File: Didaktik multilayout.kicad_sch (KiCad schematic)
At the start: 119 parts, among them J1 Conn_01x04_MountingPin, J2 AVR-ISP-6, SW1 SW_Push_45deg, SW10 SW_Push_45deg, SW11 SW_Push_45deg, SW12 SW_Push_45deg, SW13 SW_Push_45deg, SW14 SW_Push_45deg, SW15 SW_Push_45deg, SW16 SW_Push_45deg, SW17 SW_Push_45deg, SW18 SW_Push_45deg, SW19 SW_Push_45deg, SW2 SW_Push_45deg, SW20 SW_Push_45deg, SW21 SW_Push_45deg, SW22 SW_Push_45deg, SW23 SW_Push_45deg, SW24 SW_Push_45deg, SW25 SW_Push_45deg, SW26 SW_Push_45deg, SW27 SW_Push_45deg, SW28 SW_Push_45deg, SW29 SW_Push_45deg, SW3 SW_Push_45deg, SW30 SW_Push_45deg, SW31 SW_Push_45deg, SW31a1 SW_Push_45deg, SW32 SW_Push_45deg, SW32a1 SW_Push_45deg, SW33 SW_Push_45deg, SW33a1 SW_Push_45deg, SW34 SW_Push_45deg, SW34a1 SW_Push_45deg, SW34b1 SW_Push_45deg, SW35 SW_Push_45deg, SW35a1 SW_Push_45deg, SW35b1 SW_Push_45deg, SW35c1 SW_Push_45deg, SW36 SW_Push_45deg, SW36a1 SW_Push_45deg, SW36b1 SW_Push_45deg, SW36c1 SW_Push_45deg, SW37 SW_Push_45deg, SW37a1 SW_Push_45deg, SW37b1 SW_Push_45deg, SW38 SW_Push_45deg, SW38a1 SW_Push_45deg, SW39 SW_Push_45deg, SW39a1 SW_Push_45deg, SW4 SW_Push_45deg, SW40 SW_Push_45deg, SW40a1 SW_Push_45deg, SW5 SW_Push_45deg, SW6 SW_Push_45deg, SW7 SW_Push_45deg, SW8 SW_Push_45deg, SW9 SW_Push_45deg, U1 ATmega32U4-M, Y1 Crystal_GND24_Small

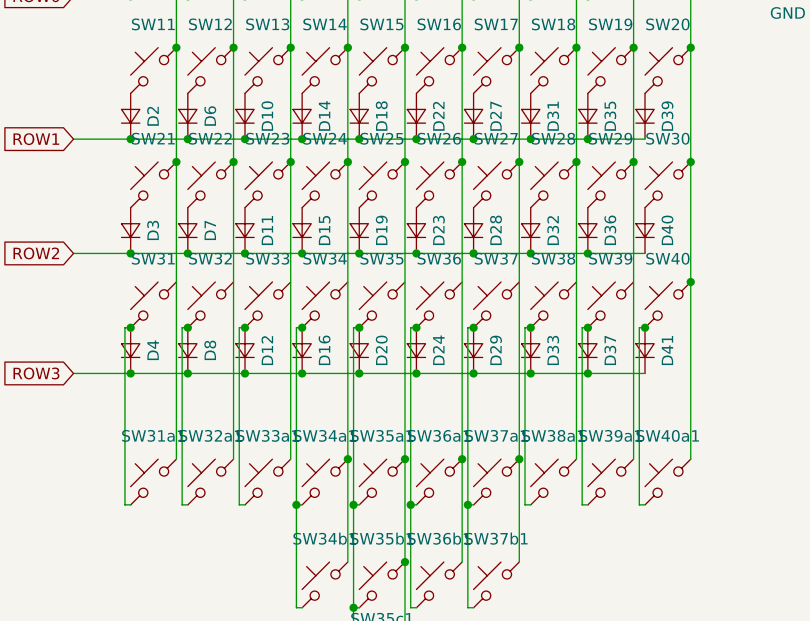
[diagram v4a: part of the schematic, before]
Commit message: routing new simpler matrix on pcb
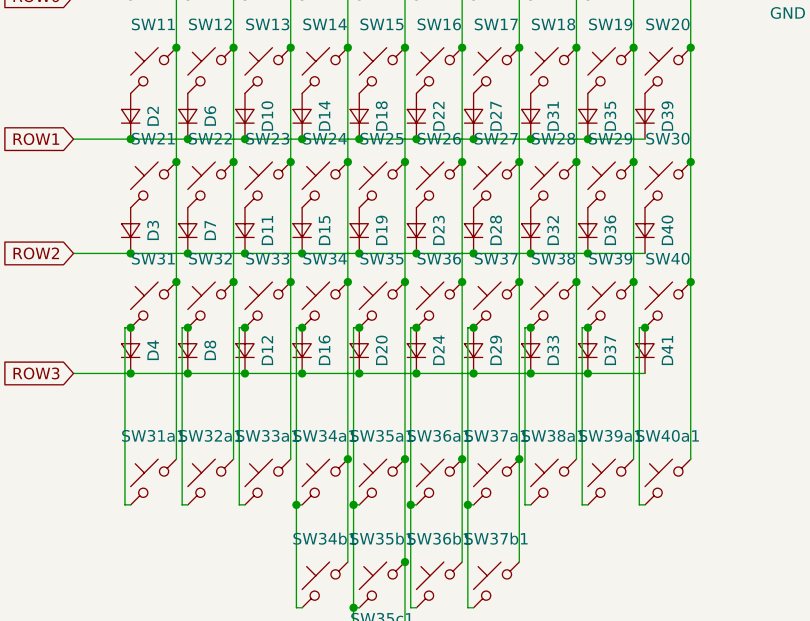
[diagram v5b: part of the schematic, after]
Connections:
- net COL0: now also SW31.1
- net COL1: now also SW32.1
- net COL2: now also SW33.1
- net COL3: now also SW34.1
- net COL4: now also SW35.1
- net COL5: now also SW36.1
- net COL6: now also SW37.1
- net COL7: now also SW38.1
- net COL8: now also SW39.1
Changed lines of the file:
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@@
   (junction (at 116.84 156.21) (diameter 0) (color 0 0 0 0)
   )
+  (junction (at 214.63 83.185) (diameter 0) (color 0 0 0 0)
+  )
   (junction (at 156.21 160.655) (diameter 0) (color 0 0 0 0)
   )
@@
   (junction (at 201.93 41.275) (diameter 0) (color 0 0 0 0)
   )
+  (junction (at 189.23 83.185) (diameter 0) (color 0 0 0 0)
+  )
   (junction (at 116.84 151.13) (diameter 0) (color 0 0 0 0)
   )
@@
   (junction (at 152.4 155.575) (diameter 0) (color 0 0 0 0)
   )
+  (junction (at 176.53 83.185) (diameter 0) (color 0 0 0 0)
+  )
   (junction (at 171.45 80.01) (diameter 0) (color 0 0 0 0)
   )
@@
   (junction (at 177.8 93.345) (diameter 0) (color 0 0 0 0)
   )
+  (junction (at 201.93 83.185) (diameter 0) (color 0 0 0 0)
+  )
   (junction (at 209.55 51.435) (diameter 0) (color 0 0 0 0)
   )
@@
   (junction (at 171.45 67.31) (diameter 0) (color 0 0 0 0)
   )
+  (junction (at 170.18 83.185) (diameter 0) (color 0 0 0 0)
+  )
   (junction (at 196.85 88.265) (diameter 0) (color 0 0 0 0)
   )
@@
   (junction (at 160.02 160.655) (diameter 0) (color 0 0 0 0)
   )
+  (junction (at 195.58 83.185) (diameter 0) (color 0 0 0 0)
+  )
+  (junction (at 165.1 88.265) (diameter 0) (color 0 0 0 0)
+  )
   (junction (at 227.33 41.275) (diameter 0) (color 0 0 0 0)
   )
@@
   (junction (at 190.5 93.345) (diameter 0) (color 0 0 0 0)
   )
-  (junction (at 165.1 88.265) (diameter 0) (color 0 0 0 0)
-  )
   (junction (at 50.8 24.13) (diameter 0) (color 0 0 0 0)
   )
@@
   (junction (at 214.63 69.85) (diameter 0) (color 0 0 0 0)
   )
+  (junction (at 208.28 83.185) (diameter 0) (color 0 0 0 0)
+  )
   (junction (at 208.28 102.87) (diameter 0) (color 0 0 0 0)
   )
@@
   (junction (at 148.59 160.655) (diameter 0) (color 0 0 0 0)
   )
+  (junction (at 220.98 83.185) (diameter 0) (color 0 0 0 0)
+  )
   (junction (at 165.1 67.31) (diameter 0) (color 0 0 0 0)
   )
   (junction (at 182.88 57.15) (diameter 0) (color 0 0 0 0)
   )
+  (junction (at 182.88 83.185) (diameter 0) (color 0 0 0 0)
+  )
   (wire (pts (xy 183.515 107.95) (xy 184.15 107.95))
     (stroke (width 0) (type default) (color 0 0 0 0))
@@
     (stroke (width 0) (type default) (color 0 0 0 0))
   )
+  (wire (pts (xy 201.93 83.185) (xy 201.93 102.87))
+    (stroke (width 0) (type default) (color 0 0 0 0))
+  )
   (wire (pts (xy 189.865 136.525) (xy 196.215 136.525))
     (stroke (width 0) (type default) (color 0 0 0 0))
@@
     (stroke (width 0) (type default) (color 0 0 0 0))
   )
-  (wire (pts (xy 220.98 69.85) (xy 220.98 102.87))
+  (wire (pts (xy 220.98 69.85) (xy 220.98 83.185))
     (stroke (width 0) (type default) (color 0 0 0 0))
   )
@@
     (stroke (width 0) (type default) (color 0 0 0 0))
   )
-  (wire (pts (xy 170.18 69.85) (xy 170.18 102.87))
+  (wire (pts (xy 195.58 83.185) (xy 195.58 102.87))
+    (stroke (width 0) (type default) (color 0 0 0 0))
+  )
+  (wire (pts (xy 170.18 69.85) (xy 170.18 83.185))
     (stroke (width 0) (type default) (color 0 0 0 0))
   )
@@
     (stroke (width 0) (type default) (color 0 0 0 0))
   )
-  (wire (pts (xy 195.58 69.85) (xy 195.58 102.87))
+  (wire (pts (xy 195.58 69.85) (xy 195.58 83.185))
     (stroke (width 0) (type default) (color 0 0 0 0))
   )
@@
     (stroke (width 0) (type default) (color 0 0 0 0))
   )
-  (wire (pts (xy 214.63 69.85) (xy 214.63 102.87))
+  (wire (pts (xy 214.63 69.85) (xy 214.63 83.185))
+    (stroke (width 0) (type default) (color 0 0 0 0))
+  )
+  (wire (pts (xy 208.28 83.185) (xy 208.28 102.87))
     (stroke (width 0) (type default) (color 0 0 0 0))
   )
@@
     (stroke (width 0) (type default) (color 0 0 0 0))
   )
-  (wire (pts (xy 208.28 69.85) (xy 208.28 102.87))
+  (wire (pts (xy 208.28 69.85) (xy 208.28 83.185))
     (stroke (width 0) (type default) (color 0 0 0 0))
   )
@@
     (stroke (width 0) (type default) (color 0 0 0 0))
   )
-  (wire (pts (xy 182.88 69.85) (xy 182.88 102.87))
-    (stroke (width 0) (type default) (color 0 0 0 0))
-  )
-  (wire (pts (xy 201.93 69.85) (xy 201.93 102.87))
+  (wire (pts (xy 182.88 69.85) (xy 182.88 83.185))
+    (stroke (width 0) (type default) (color 0 0 0 0))
+  )
+  (wire (pts (xy 201.93 69.85) (xy 201.93 83.185))
     (stroke (width 0) (type default) (color 0 0 0 0))
   )
@@
     (stroke (width 0) (type default) (color 0 0 0 0))
   )
+  (wire (pts (xy 220.98 83.185) (xy 220.98 102.87))
+    (stroke (width 0) (type default) (color 0 0 0 0))
+  )
   (wire (pts (xy 131.445 186.69) (xy 135.255 186.69))
     (stroke (width 0) (type default) (color 0 0 0 0))
@@
     (stroke (width 0) (type default) (color 0 0 0 0))
   )
-  (wire (pts (xy 176.53 69.85) (xy 176.53 102.87))
+  (wire (pts (xy 176.53 69.85) (xy 176.53 83.185))
     (stroke (width 0) (type default) (color 0 0 0 0))
   )
@@
     (stroke (width 0) (type default) (color 0 0 0 0))
   )
+  (wire (pts (xy 170.18 83.185) (xy 170.18 102.87))
+    (stroke (width 0) (type default) (color 0 0 0 0))
+  )
   (wire (pts (xy 195.58 34.925) (xy 195.58 41.275))
     (stroke (width 0) (type default) (color 0 0 0 0))
@@
     (stroke (width 0) (type default) (color 0 0 0 0))
   )
+  (wire (pts (xy 176.53 83.185) (xy 176.53 102.87))
+    (stroke (width 0) (type default) (color 0 0 0 0))
+  )
   (wire (pts (xy 227.33 41.275) (xy 227.33 57.15))
     (stroke (width 0) (type default) (color 0 0 0 0))
@@
     (stroke (width 0) (type default) (color 0 0 0 0))
   )
+  (wire (pts (xy 189.23 83.185) (xy 189.23 102.87))
+    (stroke (width 0) (type default) (color 0 0 0 0))
+  )
   (wire (pts (xy 209.55 80.01) (xy 203.2 80.01))
     (stroke (width 0) (type default) (color 0 0 0 0))
@@
     (stroke (width 0) (type default) (color 0 0 0 0))
   )
+  (wire (pts (xy 214.63 83.185) (xy 214.63 102.87))
+    (stroke (width 0) (type default) (color 0 0 0 0))
+  )
   (wire (pts (xy 164.465 107.95) (xy 165.1 107.95))
     (stroke (width 0) (type default) (color 0 0 0 0))
@@
     (stroke (width 0) (type default) (color 0 0 0 0))
   )
+  (wire (pts (xy 182.88 83.185) (xy 182.88 102.87))
+    (stroke (width 0) (type default) (color 0 0 0 0))
+  )
   (wire (pts (xy 170.18 34.925) (xy 170.18 41.275))
     (stroke (width 0) (type default) (color 0 0 0 0))
@@
     (stroke (width 0) (type default) (color 0 0 0 0))
   )
-  (wire (pts (xy 189.23 69.85) (xy 189.23 102.87))
-    (stroke (width 0) (type default) (color 0 0 0 0))
-  )
+  (wire (pts (xy 189.23 69.85) (xy 189.23 83.185))
+    (stroke (width 0) (type default) (color 0 0 0 0))
+  )

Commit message: pcb copy, footprint revision, rerouting needed
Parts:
- SW1, SW10, SW11, SW12, SW13, SW14, SW15, SW16, SW17, SW18, SW19, SW2, SW20, SW21, SW22, SW23, SW24, SW25, SW26, SW27, SW28, SW29, SW3, SW30, SW31a1, SW32, SW32a1, SW33, SW33a1, SW34, SW34a1, SW35, SW36, SW37, SW37a1, SW38, SW38a1, SW39, SW39a1, SW4, SW40a1, SW5, SW6, SW7, SW8, SW9: footprint Keebio-Parts:MX-Alps-Choc-1U-NoLED -> MX_Only:MXOnly-1U-NoLED
- SW31, SW35a1, SW36a1, SW40: footprint Keebio-Parts:MX-Alps-Choc-1.5U-NoLED -> MX_Only:MXOnly-1.5U-NoLED
- SW34b1, SW37b1: footprint Keebio-Parts:MX-Alps-Choc-3U-NoLED-StabFlip -> MX_Only:MXOnly-3U-ReversedStabilizers-NoLED
- SW35b1, SW36b1: footprint Keebio-Parts:MX-Alps-Choc-2U-NoLED-StabFlip -> MX_Only:MXOnly-2U-ReversedStabilizers-NoLED
- SW35c1: footprint Keebio-Parts:MX-Alps-Choc-6U-NoLED-StabFlip -> MX_Only:MXOnly-6U-Centered-ReversedStabilizers-NoLED
- SW36c1: footprint Keebio-Parts:MX-Alps-Choc-7U-NoLED-StabFlip -> MX_Only:MXOnly-7U-ReversedStabilizers-NoLED

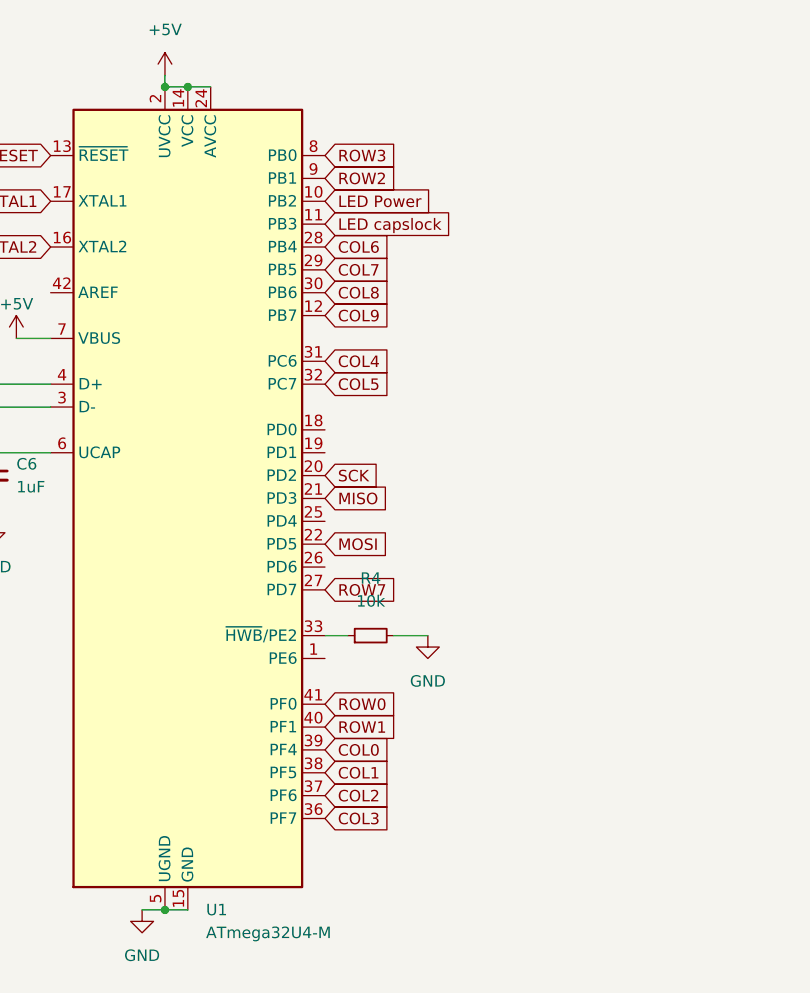
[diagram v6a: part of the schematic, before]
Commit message: full routing of mcu & matrix
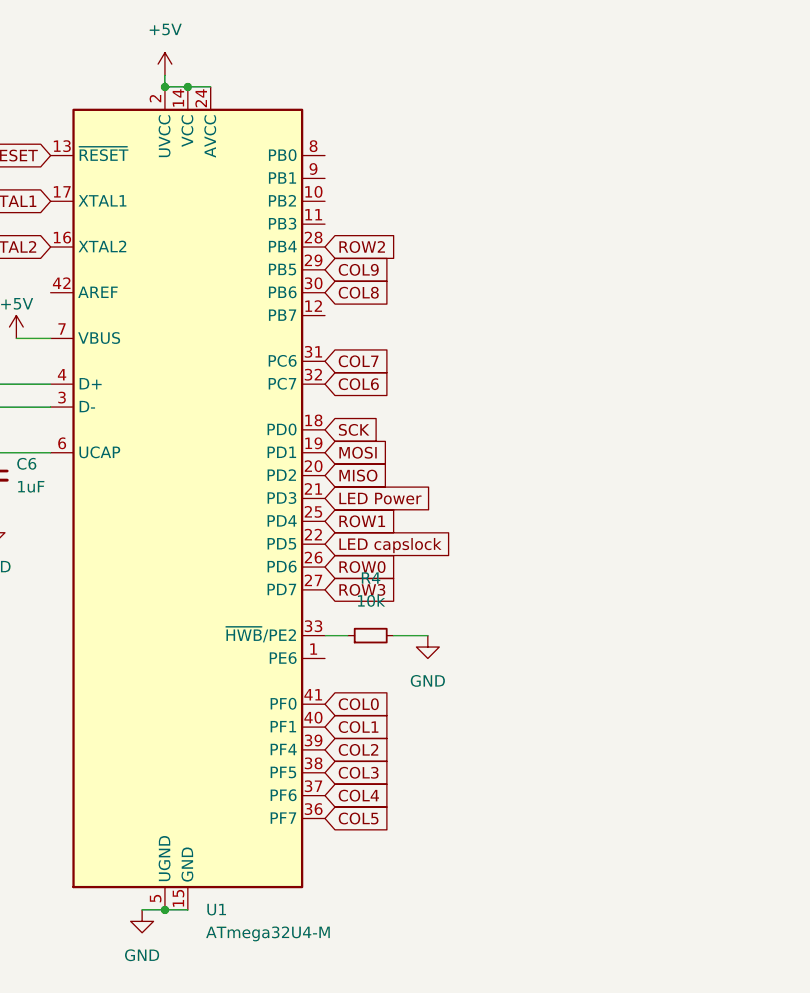
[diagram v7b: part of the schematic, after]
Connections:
- net ROW7 is gone; now on net ROW3: U1.27 (PD7)
- net COL0: now also U1.41 (PF0); no longer U1.39 (PF4)
- net COL1: now also U1.40 (PF1); no longer U1.38 (PF5)
- net COL2: now also U1.39 (PF4); no longer U1.37 (PF6)
- net COL3: now also U1.38 (PF5); no longer U1.36 (PF7)
- net COL4: now also U1.37 (PF6); no longer U1.31 (PC6)
- net COL5: now also U1.36 (PF7); no longer U1.32 (PC7)
- net COL6: now also U1.32 (PC7); no longer U1.28 (PB4)
- net COL7: now also U1.31 (PC6); no longer U1.29 (PB5)
- net COL9: now also U1.29 (PB5); no longer U1.12 (PB7)
- net LED Power: now also U1.21 (PD3); no longer U1.10 (PB2)
- net LED capslock: now also U1.22 (PD5); no longer U1.11 (PB3)
- net MISO: now also U1.20 (PD2); no longer U1.21 (PD3)
- net MOSI: now also U1.19 (PD1); no longer U1.22 (PD5)
- net ROW0: now also U1.26 (PD6); no longer U1.41 (PF0)
- net ROW1: now also U1.25 (PD4); no longer U1.40 (PF1)
- net ROW2: now also U1.28 (PB4); no longer U1.9 (PB1)
- net ROW3: no longer U1.8 (PB0)
- net SCK: now also U1.18 (PD0); no longer U1.20 (PD2)
